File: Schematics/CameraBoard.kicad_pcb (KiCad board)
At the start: 2 copper layers, 66.5 x 50.9 mm, 70 parts, among them J2 USB_C_Receptacle, U1 STM32F405RGTx, U2 TPS22917DBVR, U3 TPS22917DBVR, U5 AMS1117-3.3, U6 TPS22917DBVR, U8 SN65HVD230

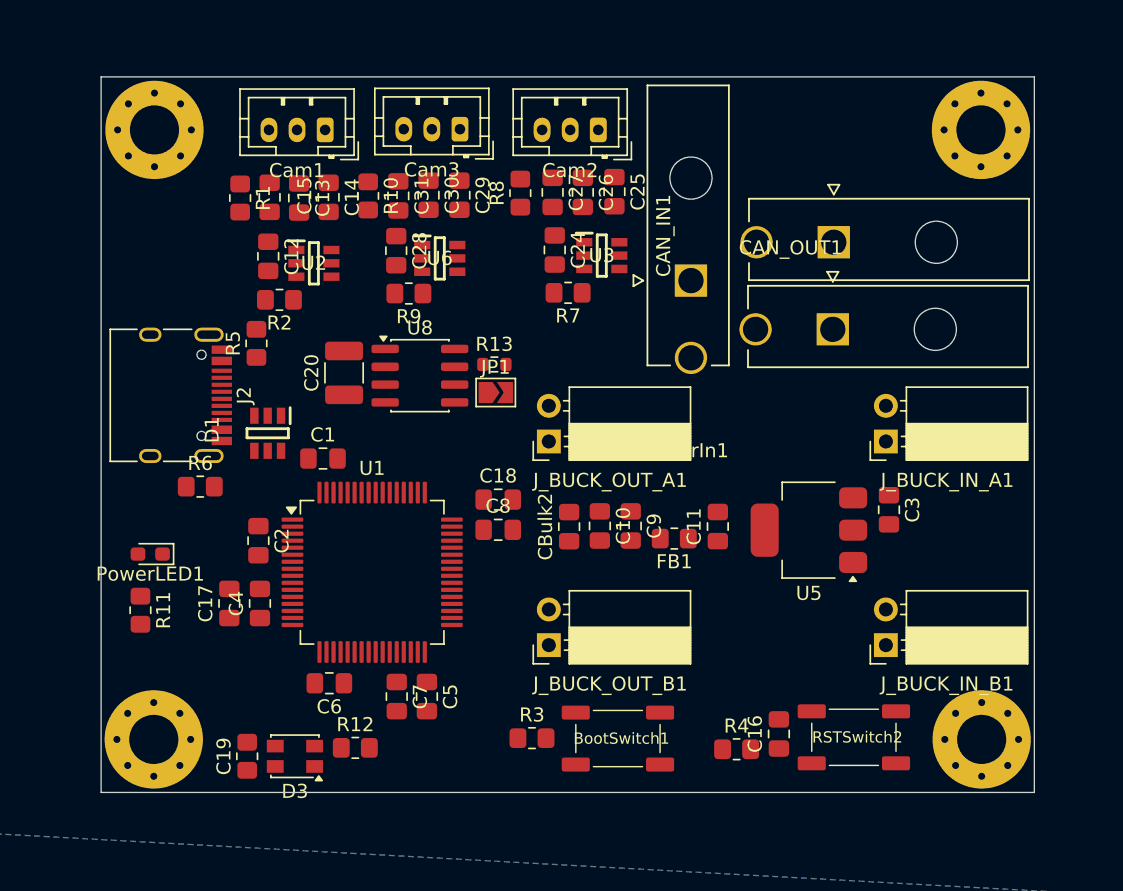
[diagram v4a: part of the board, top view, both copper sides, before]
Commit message: fixed silkscreen
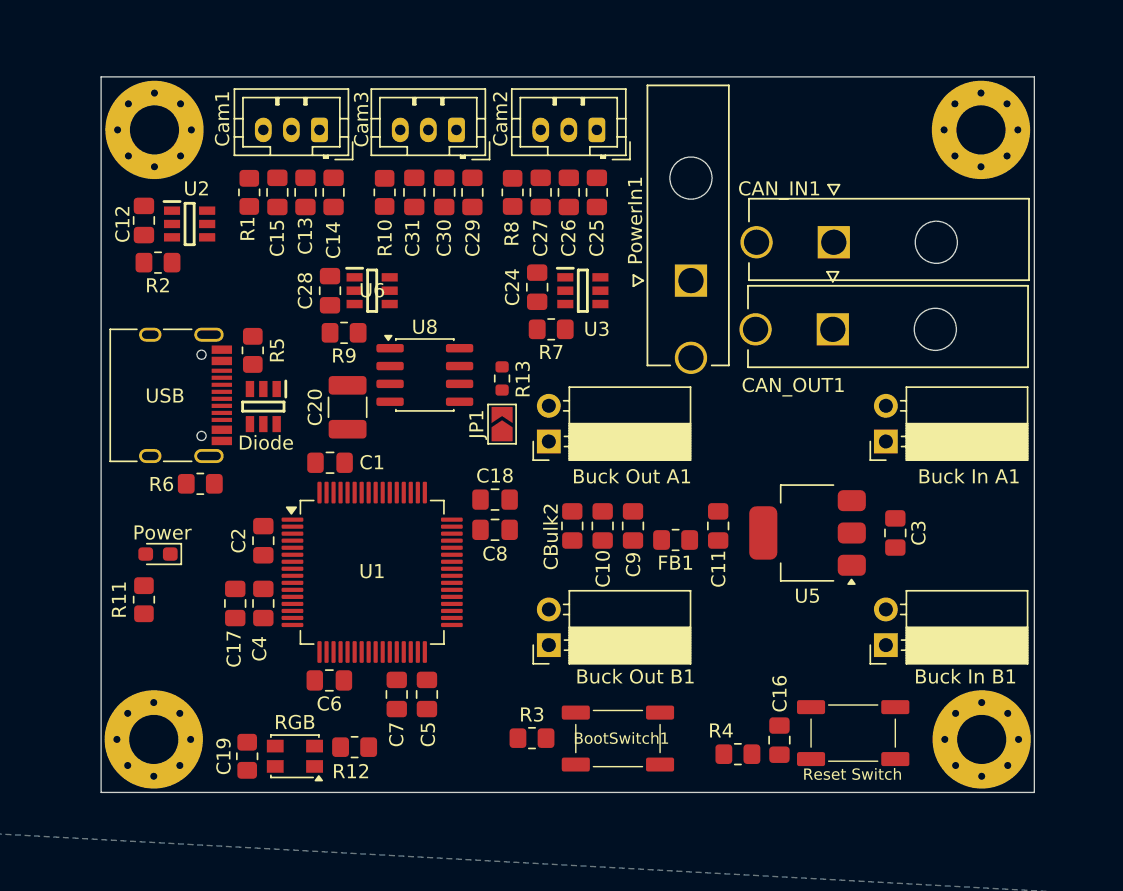
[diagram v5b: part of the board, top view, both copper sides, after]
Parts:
- Buck In A1: renamed from J_BUCK_IN_A1
- Buck In B1: renamed from J_BUCK_IN_B1
- Buck Out A1: renamed from J_BUCK_OUT_A1
- Buck Out B1: renamed from J_BUCK_OUT_B1
- Reset Switch: renamed from RSTSwitch2
- moved U2 9.28 mm to (60.0, 74.5)
- moved C12 9.21 mm to (56.8, 74.2)
- moved R2 9.05 mm to (57.8, 77.2)
- moved C28 5.51 mm to (70.0, 79.2)
- moved R9 5.40 mm to (71.0, 82.2)
- moved U6 5.33 mm to (73.0, 79.2)
- moved C24 2.93 mm to (84.8, 79.0)
- moved R7 2.86 mm to (85.8, 82.0)
- moved U3 2.84 mm to (88.0, 79.2)
- moved C20 2.46 mm to (71.2, 87.5)
- moved JP1 2.29 mm to (82.2, 88.8), turned to 90 degrees
- moved Diode 1.93 mm to (65.2, 87.5)
- moved C3 1.71 mm to (110.2, 96.5)
- moved C25 1.25 mm to (89.0, 72.2)
- moved R10 1.20 mm to (73.9, 72.2)
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- renumbered D1 to Diode, PowerLED1 to Power, D3 to RGB, J2 to USB
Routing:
- net +3.3V: track 0.76 -> 0.00 mm

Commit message: began routing
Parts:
- moved C5 1.60 mm to (78.5, 108.0)
- moved C7 1.60 mm to (76.3, 108.0)
- moved C8 1.25 mm to (81.5, 97.5), turned to -90 degrees
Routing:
- net +3.3V: track 0.00 -> 115.9 mm
- net +5V: track 0.00 -> 103.0 mm
- net /Power/VBAT: track 0.00 -> 37.1 mm
- net /Camera_left/<NO NET>: track 0.00 -> 17.8 mm
- net GND: track 0.00 -> 17.7 mm
- net Net-(U1-VCAP_2): track 0.00 -> 3.00 mm
- net Net-(U1-VCAP_1): track 0.00 -> 2.03 mm
- net /Camera_left/CAM_L_PWN_EN: track 0.00 -> 1.80 mm

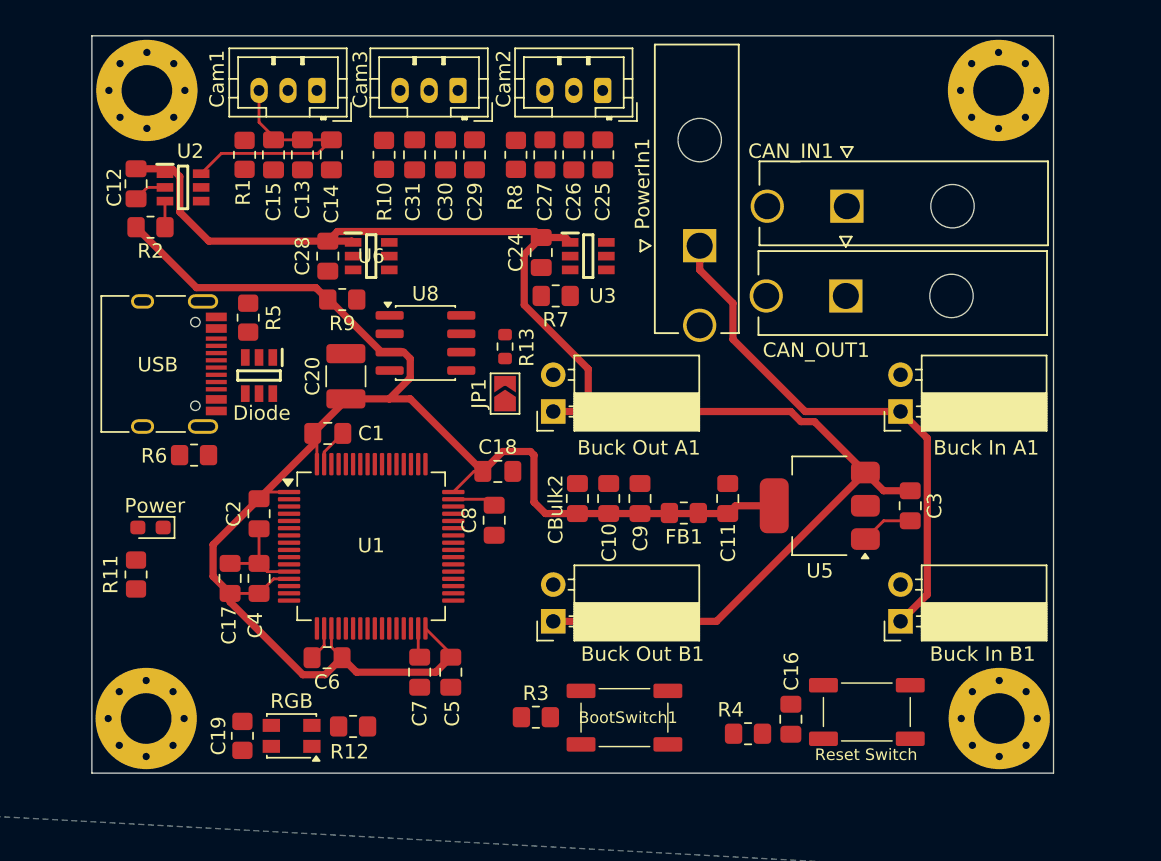
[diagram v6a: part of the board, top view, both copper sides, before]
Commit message: routing taking place only USB to do
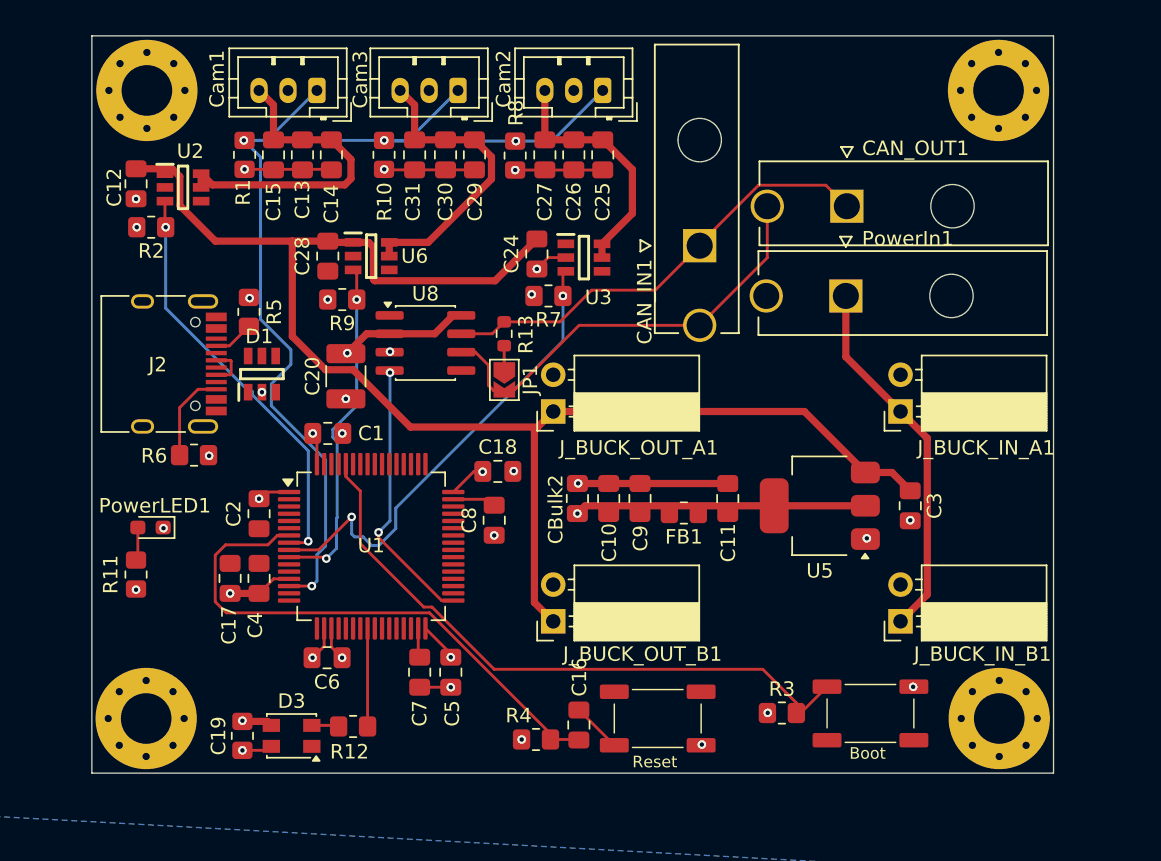
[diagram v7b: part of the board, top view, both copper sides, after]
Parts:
- J_BUCK_IN_A1: renamed from Buck In A1
- J_BUCK_IN_B1: renamed from Buck In B1
- J_BUCK_OUT_A1: renamed from Buck Out A1
- J_BUCK_OUT_B1: renamed from Buck Out B1
- Reset: renamed from Reset Switch
- moved Boot 17.0 mm to (107.5, 110.8), turned to 180 degrees
- moved R3 17.0 mm to (101.4, 110.8)
- moved C16 14.7 mm to (87.3, 111.7)
- moved R4 14.7 mm to (84.4, 112.7)
- moved Reset 14.5 mm to (92.8, 111.2), turned to 180 degrees
- moved PowerIn1 10.7 mm to (105.8, 82.0), turned to 90 degrees
- moved CAN_IN1 10.5 mm to (95.7, 78.5), turned to 180 degrees
- moved CAN_OUT1 6.20 mm to (105.9, 75.8)
- moved JP1 0.95 mm to (82.2, 87.8), turned to -90 degrees
- moved R13 0.89 mm to (82.2, 84.6)
- moved R7 0.50 mm to (85.2, 82.0)
- moved R5 0.40 mm to (64.5, 83.1)
- moved C24 0.32 mm to (84.5, 79.1)
- moved U3 0.32 mm to (87.7, 79.3)
- moved D1 0.22 mm to (65.5, 87.4), turned to 90 degrees
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- renumbered BootSwitch1 to Boot, Diode to D1, RGB to D3, USB to J2, Power to PowerLED1
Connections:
- net /MCU/UART_DEBUG_RX renamed UART_DEBUG_RX
- net /MCU/VBUS renamed VBUS
- C19 pad 2: +5V -> +3.3V
- Cam1 pad 1: /Camera_left/CAM_UART_TX -> CAM_UART_TX
- Cam2 pad 1: /Camera_right/CAM_UART_TX -> CAM_UART_TX
- Cam3 pad 1: /Camera_center/CAM_UART_TX -> CAM_UART_TX
- D1 pad 1: unconnected-(D1-Pad1) -> D-
- D1 pad 3: /usb_type_c/D- -> unconnected-(D1-Pad3)
- D1 pad 4: /usb_type_c/D+ -> unconnected-(D1-Pad4)
- D1 pad 6: unconnected-(D1-Pad6) -> D+
- D3 pad 3: +5V -> +3.3V
- J2 pad A6: /usb_type_c/D+ -> D+
- J2 pad A7: /usb_type_c/D- -> D-
- J2 pad B6: /usb_type_c/D+ -> D+
- J2 pad B7: /usb_type_c/D- -> D-
- R1 pad 1: /Camera_left/CAM_UART_TX -> CAM_UART_TX
- R10 pad 1: /Camera_center/CAM_UART_TX -> CAM_UART_TX
- R2 pad 1: /Camera_left/CAM_L_PWN_EN -> CAM_L_PWN_EN
- R7 pad 1: /Camera_right/CAM_R_PWN_EN -> CAM_R_PWN_EN
- R8 pad 1: /Camera_right/CAM_UART_TX -> CAM_UART_TX
- R9 pad 1: /Camera_center/CAM_C_PWN_EN -> CAM_C_PWN_EN
- U1 pad 10: /MCU/CAM_C_PWN_EN -> CAM_C_PWN_EN
- U1 pad 14: /MCU/CAM_UART_TX -> CAM_UART_TX
- U1 pad 33: /MCU/CAN_RX_2 -> CAN_RX_2
- U1 pad 34: /MCU/CAN_TX_2 -> CAN_TX_2
- U1 pad 44: /MCU/D- -> D-
- U1 pad 45: /MCU/D+ -> D+
- U1 pad 8: /MCU/CAM_L_PWN_EN -> CAM_L_PWN_EN
- U1 pad 9: /MCU/CAM_R_PWN_EN -> CAM_R_PWN_EN
- U2 pad 3: /Camera_left/CAM_L_PWN_EN -> CAM_L_PWN_EN
- U3 pad 3: /Camera_right/CAM_R_PWN_EN -> CAM_R_PWN_EN
- U6 pad 3: /Camera_center/CAM_C_PWN_EN -> CAM_C_PWN_EN
- U8 pad 1: /Can_transceiver/CAN_TX_2 -> CAN_TX_2
- U8 pad 4: /Can_transceiver/CAN_RX_2 -> CAN_RX_2
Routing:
- net +3.3V: track 115.9 -> 39.7 mm, vias 0 -> 16
- net CAM_UART_TX: track 0.00 -> 75.6 mm, vias 0 -> 4
- net /MCU/BOOT0: track 0.00 -> 44.2 mm
- net /MCU/NRST: track 0.00 -> 38.2 mm
- net CAM_R_PWN_EN: track 0.00 -> 33.0 mm, vias 0 -> 2
- net /Can_transceiver/CANH: track 0.00 -> 31.6 mm
- net /Can_transceiver/CANL: track 0.00 -> 30.4 mm
- net GND: track 17.7 -> 47.5 mm, vias 0 -> 21
- net CAM_L_PWN_EN: track 0.00 -> 29.1 mm, vias 0 -> 2
- net CAM_C_PWN_EN: track 0.00 -> 23.8 mm, vias 0 -> 2
- net /Camera_center/<NO NET>: track 0.00 -> 21.0 mm
- net CAN_RX_2: track 0.00 -> 18.8 mm, vias 0 -> 2
- net /Camera_right/<NO NET>: track 0.00 -> 17.3 mm
- net /Power/VBAT: track 37.1 -> 25.6 mm
- net /MCU/RGB_DATA: track 0.00 -> 6.78 mm
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- added copper zone on In2.Cu, net +3.3V
- added copper zone on In1.Cu, net GND
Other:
- copper layers 2 -> 4
